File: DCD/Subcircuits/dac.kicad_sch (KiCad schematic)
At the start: 0 parts

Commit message: added DAC8811ICDGKT to library
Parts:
- added U2, U4: DAC8811ICDGKT, DGK8, symbol custom_components:DAC8811ICDGKT
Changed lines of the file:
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@@
 	(generator_version "9.0")
 	(paper "A4")
+	(symbol
+		(lib_name "DAC8811ICDGKT_1")
+		(lib_id "custom_components:DAC8811ICDGKT")
+		(at 127 95.25 0)
+		(unit 1)
+		(exclude_from_sim no)
+		(in_bom yes)
+		(on_board yes)
+		(dnp no)
+		(fields_autoplaced yes)
+		(property "Reference" "U2"
+			(at 157.48 85.09 0)
+			(effects
+				(font
+					(size 1.524 1.524)
+				)
+			)
+		)
+		(property "Value" "DAC8811ICDGKT"
+			(at 157.48 87.63 0)
+			(effects
+				(font
+					(size 1.524 1.524)
+				)
+			)
+		)
+		(property "Footprint" "DGK8"
+			(at 134.366 88.138 0)
+			(effects
+				(font
+					(size 1.27 1.27)
+					(italic yes)
+				)
+				(hide yes)
+			)
+		)
+		(property "Datasheet" "https://www.ti.com/lit/gpn/dac8811"
+			(at 133.35 83.312 0)
+			(effects
+				(font
+					(size 1.27 1.27)
+					(italic yes)
+				)
+				(hide yes)
+			)
+		)
+		(property "Description" ""
+			(at 127 95.25 0)
+			(effects
+				(font
+					(size 1.27 1.27)
+				)
+				(hide yes)
+			)
+		)
+		(pin "1"
+		)
+		(pin "6"
+		)
+		(pin "8"
+		)
+		(pin "4"
+		)
+		(pin "7"
+		)
+		(pin "3"
+		)
+		(pin "5"
+		)
+		(pin "2"
+		)
+		(instances
+			(project "DCD"
+				(path "/b8e3d55b-fa56-4199-88ad-60cfd98f56f9/6102592d-9e5a-4d16-a1d9-3adb4d835efe"
+					(reference "U2")
+					(unit 1)
+				)
+			)
+		)
+	)
+	(symbol
+		(lib_name "DAC8811ICDGKT_1")
+		(lib_id "custom_components:DAC8811ICDGKT")
+		(at 127 68.58 0)
+		(unit 1)
+		(exclude_from_sim no)
+		(in_bom yes)
+		(on_board yes)
+		(dnp no)
+		(fields_autoplaced yes)
+		(property "Reference" "U4"
+			(at 157.48 58.42 0)
+			(effects
+				(font
+					(size 1.524 1.524)
+				)
+			)
+		)
+		(property "Value" "DAC8811ICDGKT"
+			(at 157.48 60.96 0)
+			(effects
+				(font
+					(size 1.524 1.524)
+				)
+			)
+		)
+		(property "Footprint" "DGK8"
+			(at 134.366 61.468 0)
+			(effects
+				(font
+					(size 1.27 1.27)
+					(italic yes)
+				)
+				(hide yes)
+			)
+		)
+		(property "Datasheet" "https://www.ti.com/lit/gpn/dac8811"
+			(at 133.35 56.642 0)
+			(effects
+				(font
+					(size 1.27 1.27)
+					(italic yes)
+				)
+				(hide yes)
+			)
+		)
+		(property "Description" ""
+			(at 127 68.58 0)
+			(effects
+				(font
+					(size 1.27 1.27)
+				)
+				(hide yes)
+			)
+		)
+		(pin "1"
+		)
+		(pin "6"
+		)
+		(pin "8"
+		)
+		(pin "4"
+		)
+		(pin "7"
+		)
+		(pin "3"
+		)
+		(pin "5"
+		)
+		(pin "2"
+		)
+		(instances
+			(project ""
+				(path "/b8e3d55b-fa56-4199-88ad-60cfd98f56f9/6102592d-9e5a-4d16-a1d9-3adb4d835efe"
+					(reference "U4")
+					(unit 1)
+				)
+			)
+		)
+	)
 )

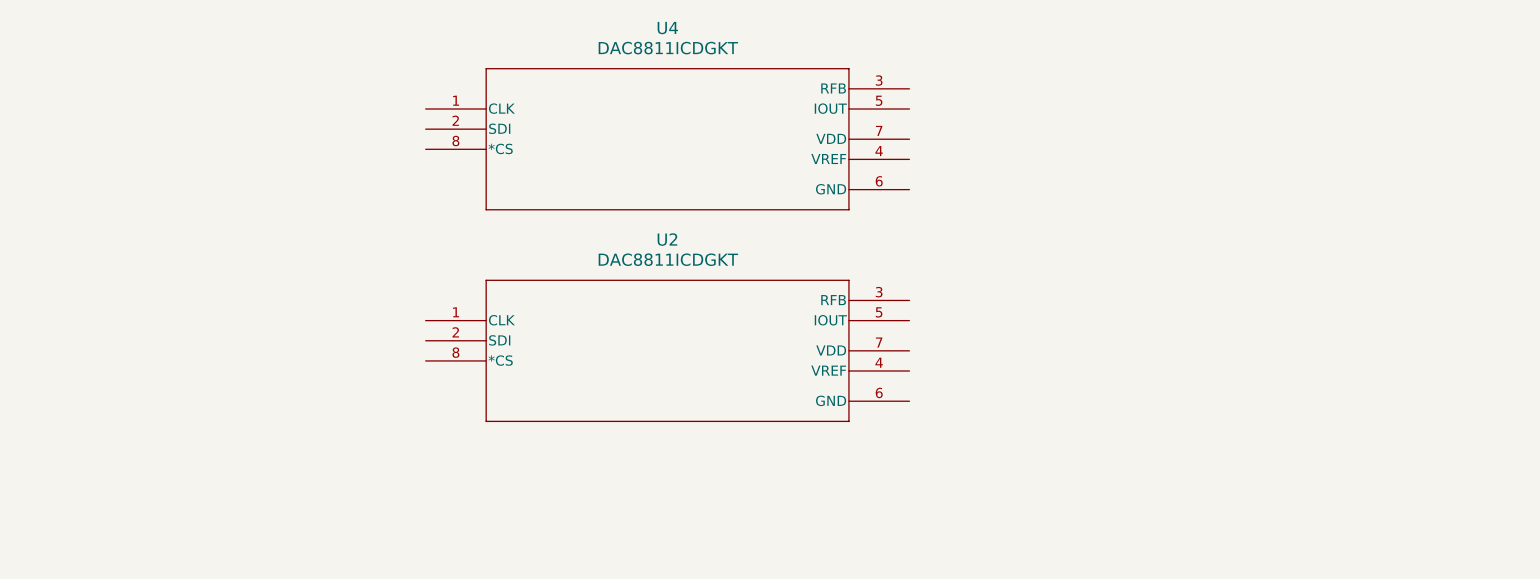
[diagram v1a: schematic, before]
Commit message: DAC schematic with opamp and top level added
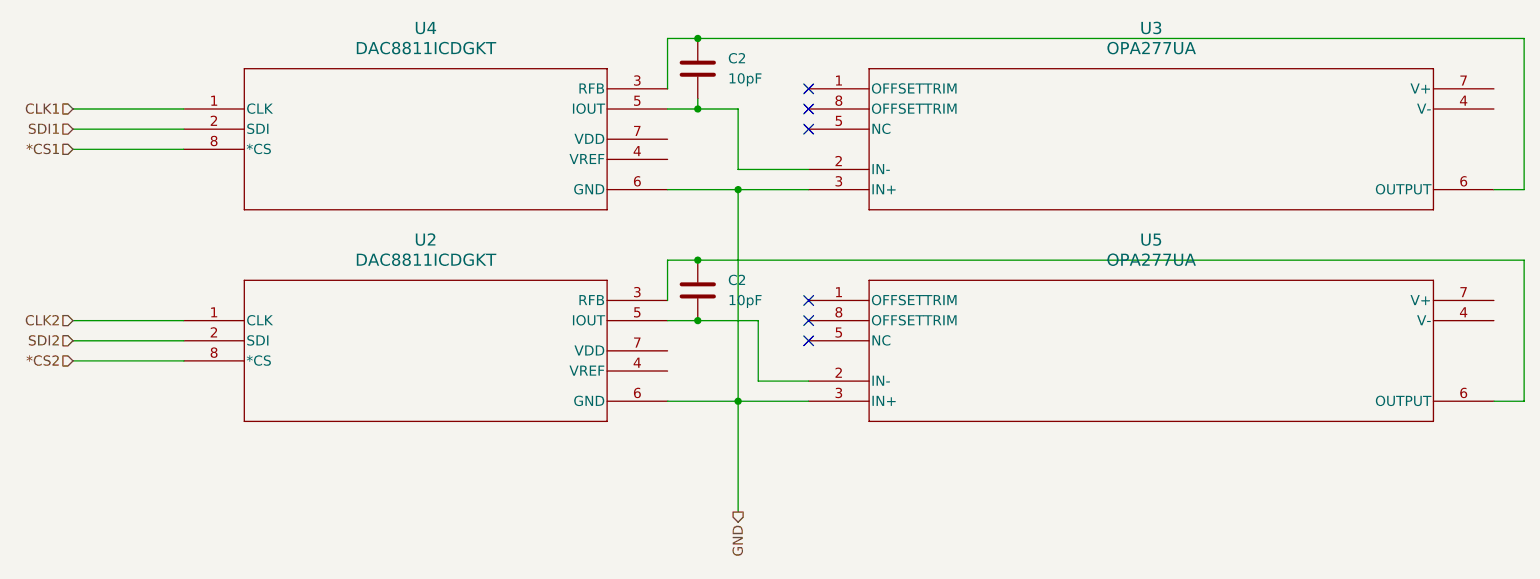
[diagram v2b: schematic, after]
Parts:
- added C2 (x2): 10pF, Capacitor_SMD:C_0603_1608Metric, symbol Device:C
- added U3, U5: OPA277UA, D8, symbol custom_components:OPA277UA
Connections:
- net CLK2: now reaches U2.1 (CLK)
- net SDI2: now reaches U2.2 (SDI)
- net at U2.3 (RFB): now also C2.1, U5.6 (OUTPUT)
- net at U2.5 (IOUT): now also C2.2, U5.2 (IN-)
- net GND: now reaches U2.6 (GND)
- net GND: now also U4.6 (GND), U3.3 (IN+), U5.3 (IN+)
- net *CS2: now reaches U2.8 (*CS)
- net CLK1: now reaches U4.1 (CLK)
- net SDI1: now reaches U4.2 (SDI)
- net at U4.3 (RFB): now also C2.1, U3.6 (OUTPUT)
- net at U4.5 (IOUT): now also C2.2, U3.2 (IN-)
- net *CS1: now reaches U4.8 (*CS)
- no-connect marks 0 -> 6
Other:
- moved on the sheet: U2, U4

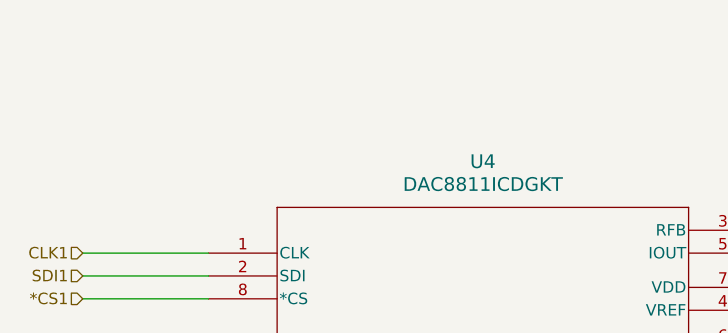
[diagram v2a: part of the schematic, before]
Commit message: Did the signal switching, finished ADC, misc changes to top
Decided to go with solder jumpers instead of power switches bc power
switches have no specs of linearity and they would add unnecessary
complexity, development time, and routing problems.

The calibration test has to be done only once and the chamber doesn't
even have to be sealed for it, so it shouldn't add too much hassle.
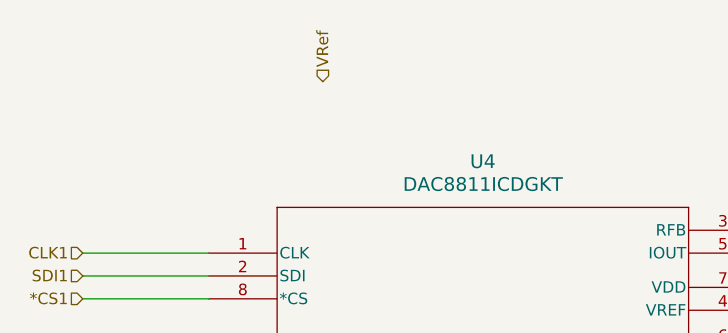
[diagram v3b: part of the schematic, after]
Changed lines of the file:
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@@
+		)
+	)
+	(hierarchical_label "VRef"
+		(shape input)
+		(at 109.22 49.53 90)
+		(effects
+			(font
+				(size 1.27 1.27)
+			)
+			(justify left)
 		)
 	)
@@
 		)
 		(instances
-			(project ""
+			(project "DCD"
 				(path "/b8e3d55b-fa56-4199-88ad-60cfd98f56f9/6102592d-9e5a-4d16-a1d9-3adb4d835efe"
 					(reference "U3")
@@
 		)
 		(instances
-			(project ""
+			(project "DCD"
 				(path "/b8e3d55b-fa56-4199-88ad-60cfd98f56f9/6102592d-9e5a-4d16-a1d9-3adb4d835efe"
 					(reference "U4")

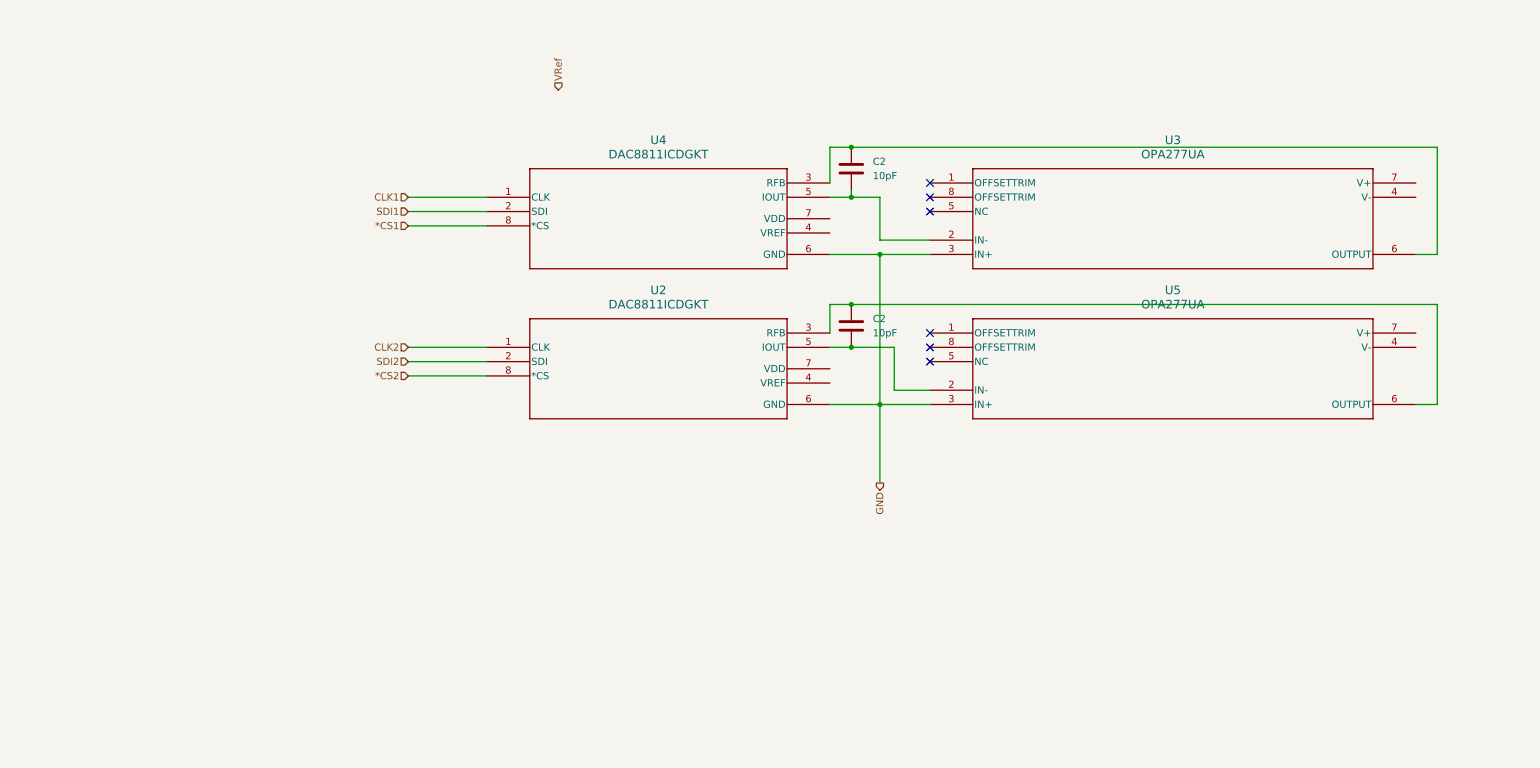
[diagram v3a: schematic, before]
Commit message: DAC design done and added component potentiometer
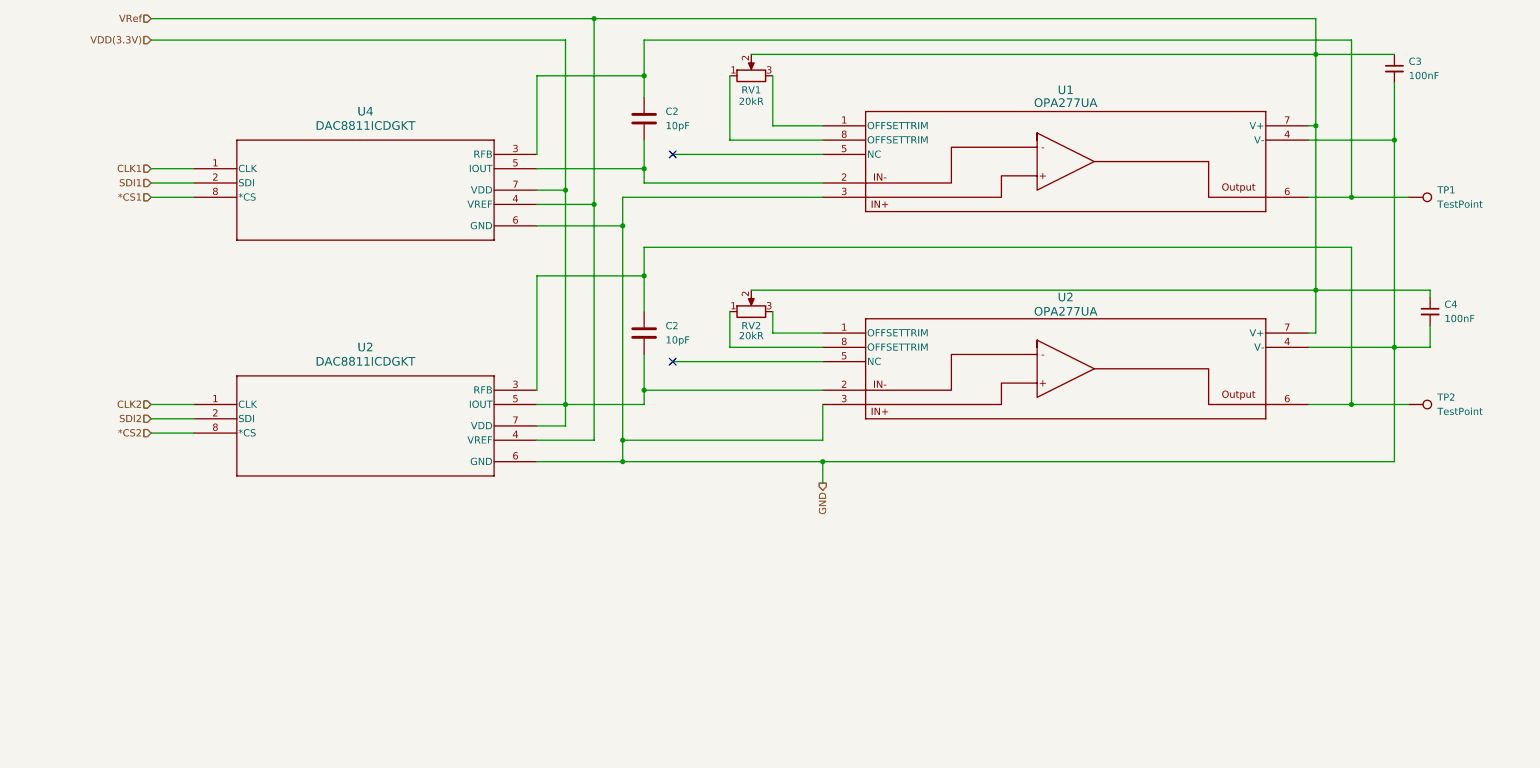
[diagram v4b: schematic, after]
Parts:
- removed U3, U5: OPA277UA, D8, symbol custom_components:OPA277UA
- added C3, C4: 100nF, Capacitor_SMD:C_0603_1608Metric, symbol Device:C_Small
- added RV1, RV2: 20kR, custom_components:IC3_3214W-1-203E_BRN, symbol Device:R_Potentiometer
- added TP1, TP2: TestPoint, TestPoint:TestPoint_Pad_D1.5mm, symbol Connector:TestPoint
- added U1, U2: OPA277UA, D8, symbol custom_components:OPA277UA
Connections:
- net GND: now also C3.2, C4.2, U1.3, U1.4 (V-), U2.3, U2.4 (V-)
- net VRef: now also U2.4 (VREF), U4.4 (VREF), C3.1, C4.1, RV1.2, RV2.2, U1.7 (V+), U2.7 (V+)
- net VDD(3.3V): now reaches C2.2, U2.5 (IOUT)
- net VDD(3.3V): now also U2.7 (VDD), U4.7 (VDD), U2.2
- net at C2.1, U2.3 (RFB): now also TP2.1, U2.6
- net at C2.1, U4.3 (RFB): now also TP1.1, U1.6
- net at C2.2, U4.5 (IOUT): now also U1.2
- new net: RV2.3, U2.1 (OFFSETTRIM)
- new net: RV2.1, U2.8 (OFFSETTRIM)
- new net: RV1.3, U1.1 (OFFSETTRIM)
- new net: RV1.1, U1.8 (OFFSETTRIM)
- no-connect marks 6 -> 2
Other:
- moved on the sheet: C2, U2, U4

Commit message: buffer added for vref to dac circuit
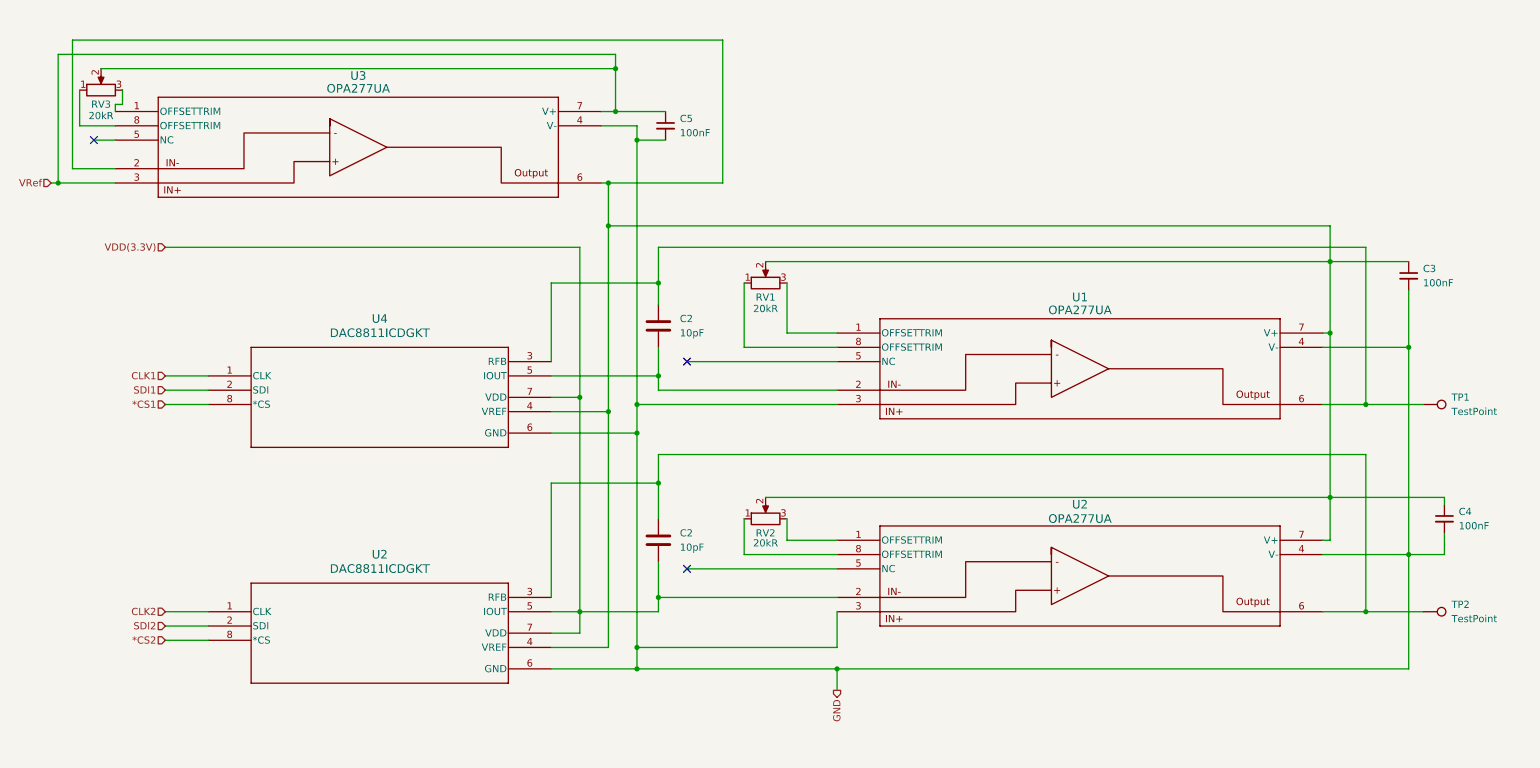
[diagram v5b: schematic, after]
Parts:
- added C5: 100nF, Capacitor_SMD:C_0603_1608Metric, symbol Device:C_Small
- added RV3: 20kR, custom_components:IC3_3214W-1-203E_BRN, symbol Device:R_Potentiometer
- added U3: OPA277UA, D8, symbol custom_components:OPA277UA
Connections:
- net GND: now also C5.2, U3.4 (V-)
- net VRef: now also C5.1, RV3.2, U3.3, U3.7 (V+); no longer C3.1, C4.1, RV1.2, RV2.2, U1.7 (V+), U2.4 (VREF), U2.7 (V+), U4.4 (VREF)
- new net: C3.1, C4.1, RV1.2, RV2.2, U1.7 (V+), U2.4 (VREF), U2.7 (V+), U3.2, U3.6, U4.4 (VREF)
- new net: RV3.1, U3.8 (OFFSETTRIM)
- new net: RV3.3, U3.1 (OFFSETTRIM)
- no-connect marks 2 -> 3
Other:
- moved on the sheet: C2, C3, C4, RV1, RV2, TP1, TP2, U1, U2, U4

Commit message: added decoupling capacitors to dac circuit
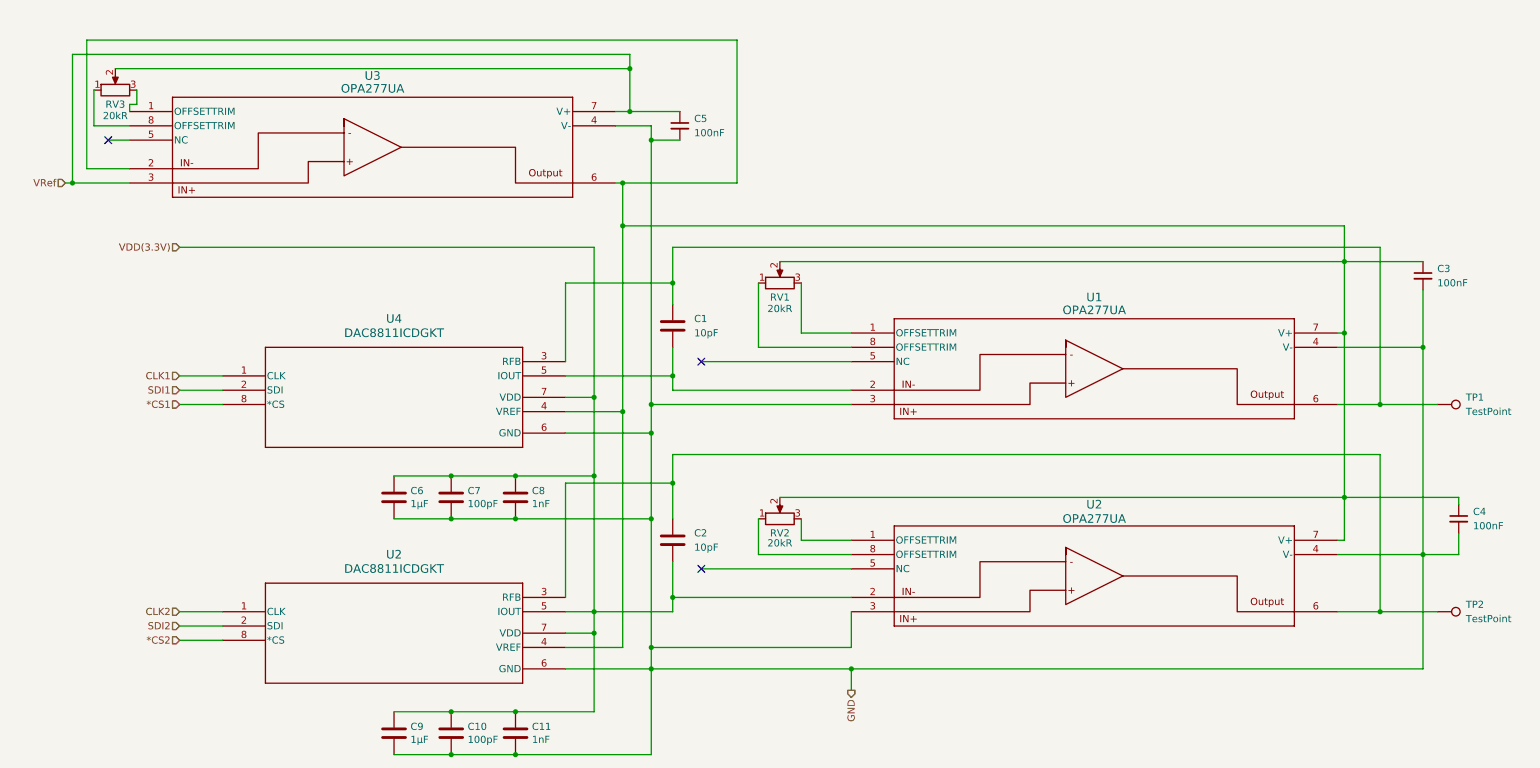
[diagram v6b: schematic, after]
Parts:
- added C10, C7: 100pF, Capacitor_SMD:C_0603_1608Metric, symbol Device:C
- added C11, C8: 1nF, Capacitor_SMD:C_0603_1608Metric, symbol Device:C
- added C6, C9: 1µF, Capacitor_SMD:C_0603_1608Metric, symbol Device:C
- renumbered C2 to C1
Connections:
- net GND: now also C10.2, C11.2, C6.2, C7.2, C8.2, C9.2
- net VDD(3.3V): now also C10.1, C11.1, C6.1, C7.1, C8.1, C9.1
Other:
- moved on the sheet: C1, C2, C3, C4, C5, RV1, RV2, RV3, TP1, TP2, U1, U2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
